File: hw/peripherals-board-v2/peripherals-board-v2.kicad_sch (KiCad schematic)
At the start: 25 parts, among them J1 Power/Motor Screw Terminal, J10 Extra Servo, J11 Conn_02x05_Odd_Even, J2 OLED, J3 BNO055, J4 LiDAR Right, J5 Radio Input, J6 LiDAR Left, J7 LiDAR Front, J8 Motor Encoder, J9 Steering Servo, SW1 Power, U1 RP2040-Zero, U4 AMS1117-5.0

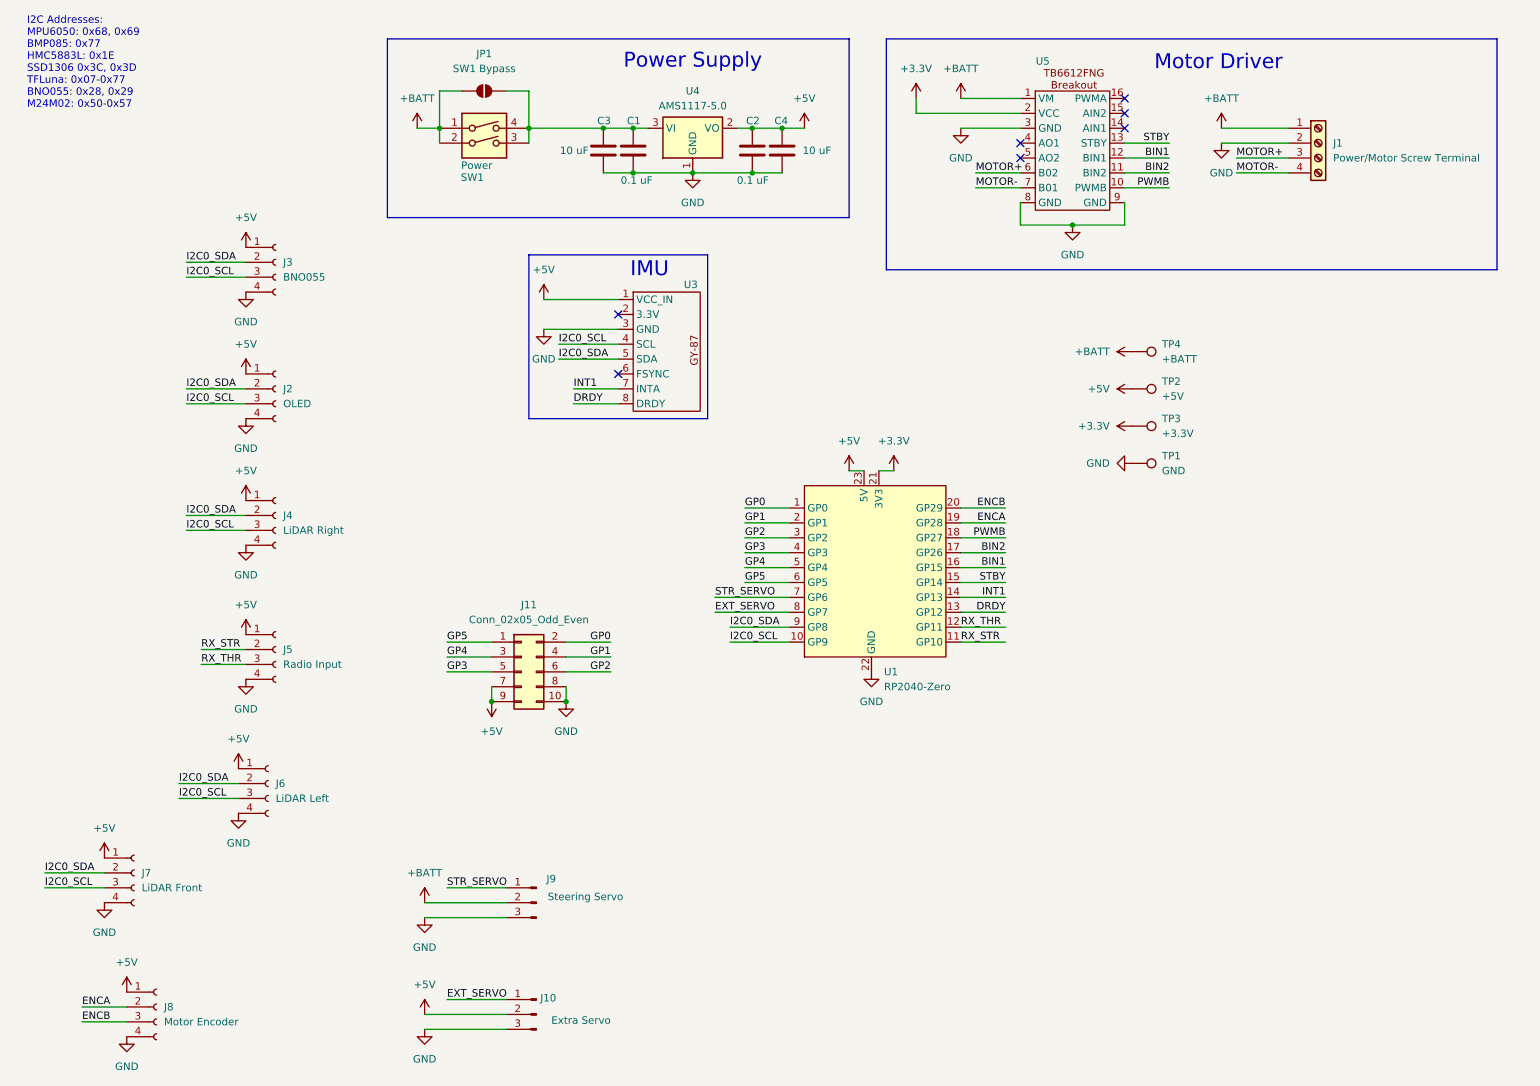
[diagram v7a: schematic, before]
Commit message: Add connector for RPLidar in schematic
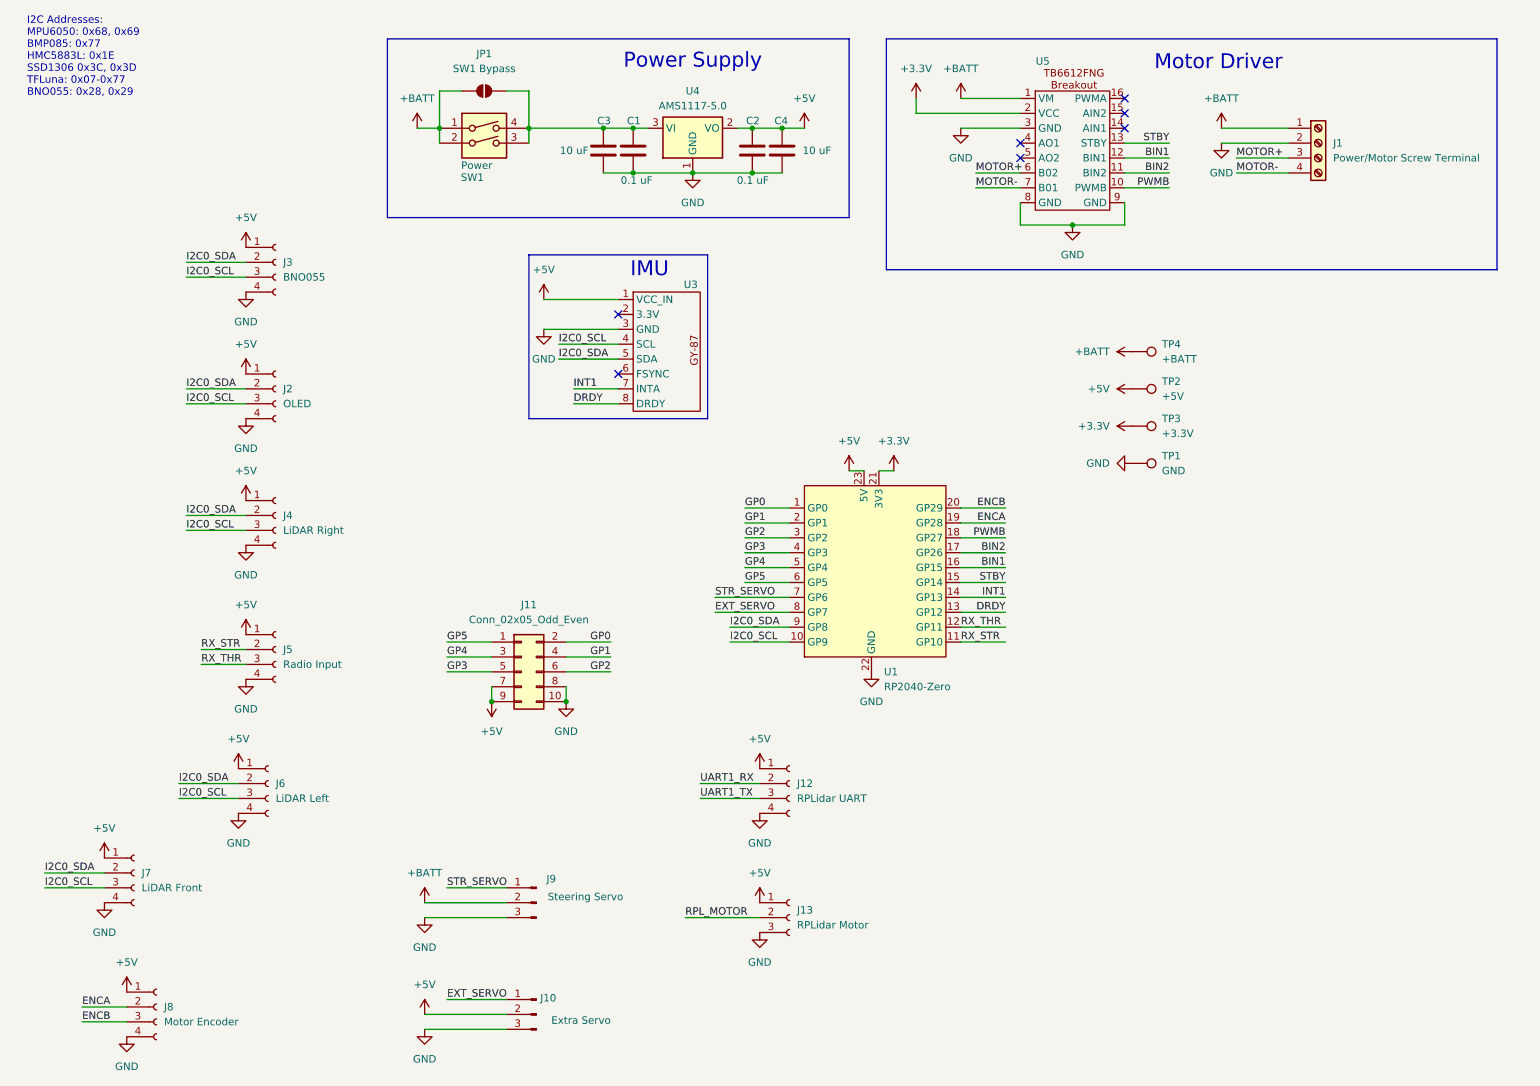
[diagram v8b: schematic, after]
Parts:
- added J12: RPLidar UART, Connector_JST:JST_EH_S4B-EH_1x04_P2.50mm_Horizontal, symbol Connector:Conn_01x04_Socket
- added J13: RPLidar Motor, symbol Connector:Conn_01x03_Socket
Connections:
- net +5V: now also J12.1 (Pin_1), J13.1 (Pin_1)
- net GND: now also J12.4 (Pin_4), J13.3 (Pin_3)
- new net RPL_MOTOR: J13.2 (Pin_2)
- new net UART1_RX: J12.2 (Pin_2)
- new net UART1_TX: J12.3 (Pin_3)
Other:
- note added: "I2C Addresses: MPU6050: 0x68, 0x69 BMP085: 0x77 HMC5883L: 0x1E SSD1306 0x3C, 0x3D TFLuna: 0x07-0x77 BNO055: 0x28, 0x29"
- note removed: "I2C Addresses: MPU6050: 0x68, 0x69 BMP085: 0x77 HMC5883L: 0x1E SSD1306 0x3C, 0x3D TFLuna: 0x07-0x77 BNO055: 0x28, 0x29 M24M02: 0x50-0x57"
